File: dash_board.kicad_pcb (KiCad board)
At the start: 2 copper layers, 100 x 100 mm, 1 part

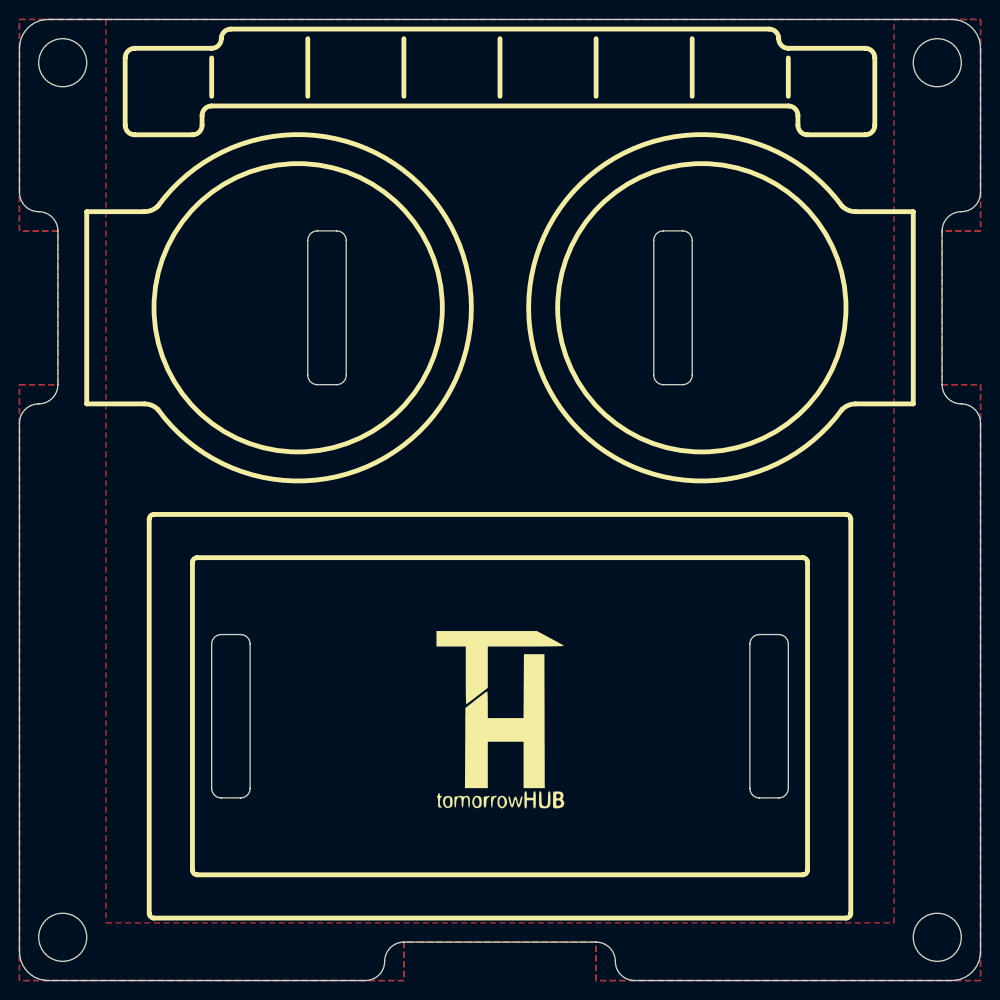
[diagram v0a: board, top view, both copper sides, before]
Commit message: modified footprints, added additional layers
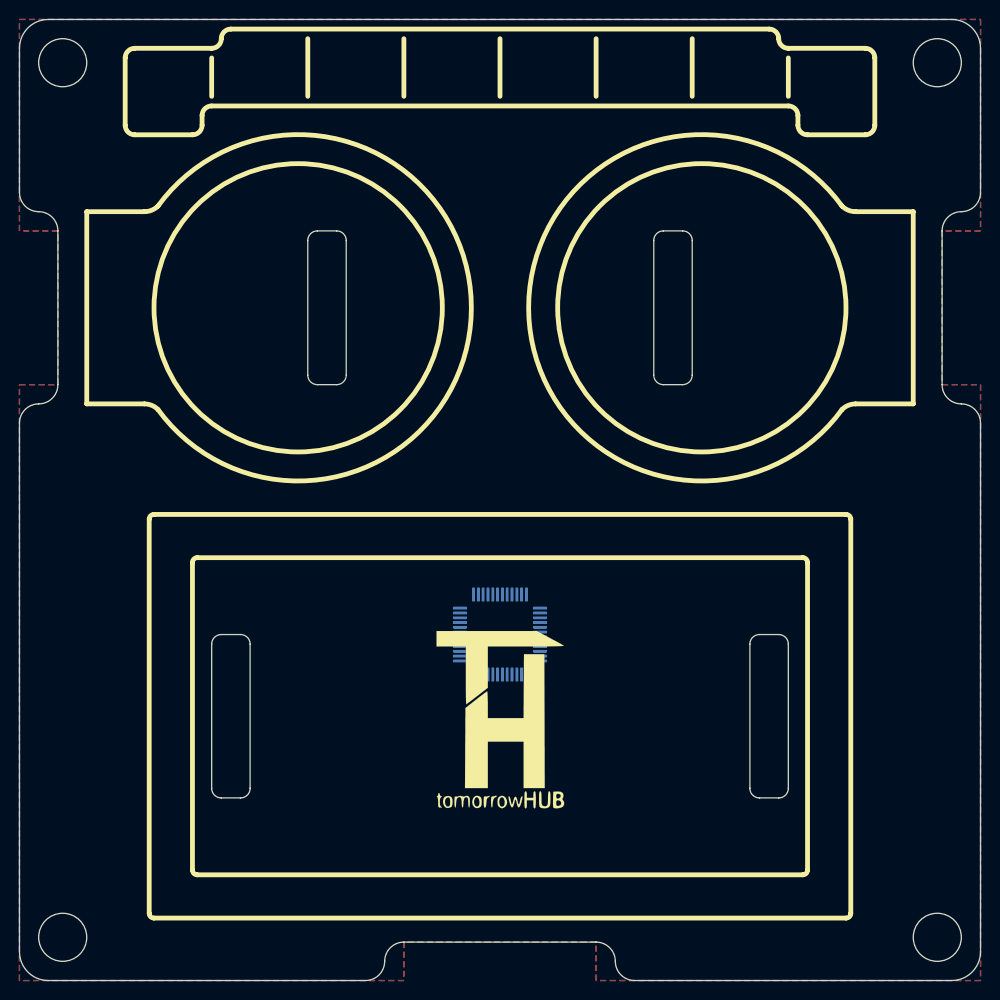
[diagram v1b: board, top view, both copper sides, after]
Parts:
- added U1: STM32F378CCTx, Package_QFP:LQFP-48_7x7mm_P0.5mm, B.Cu at (100.0, 115.0)

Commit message: some work on schematic
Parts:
- removed G***: LOGO, green_fp:tomorrow_HUB
- removed U1: STM32F378CCTx, Package_QFP:LQFP-48_7x7mm_P0.5mm
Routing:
- added copper zone on B.Cu, net GND
- added copper zone on F.Cu, net GND
- removed copper zone on B.Cu, net (none)
- removed copper zone on F.Cu, net (none)
